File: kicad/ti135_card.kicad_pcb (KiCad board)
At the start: 8 copper layers, 76 x 65.1 mm, 395 parts, among them J1 JTAG 3.3V, J101 5V0 bench input, J2 UART 3.3V, J3 2x19 1.27mm socket (bottom), J5 LCD 1x14 2.54mm, J6 2x3 1.27mm (bottom), J9 HR911130A, U1001 THGAMVG7T13BAIL, U101 NCP163ASN330T1G, U1201 SN74AXC8T245PWR, U1202 SN74AXC8T245PWR, U1203 SN74AXC8T245PWR, U1204 SN74AXC8T245PWR, U1301 SN74LV4051APWR, U1302 OPA365AIDBVR, U1303 ADS7056IRUGR, U1304 OPA365AIDBVR, U1305 OPA365AIDBVR, U1306 OPA365AIDBVR, U201 TLV62585PDRLR, U301 TLV62585PDRLR, U311 TLV62585PDRLR, U331 TLV62585PDRLR, U341 TLV62585PDRLR, U401 TPS3808G01DBVR, U501 Ti135N484I3, U601 IS25WP128-RHLE, U801 H9HCNNN8KUMLHR-NME, U901 RTL8211FDI-CG, U902 74LVC1G07GW, Y701 OT322525MJBA4SL, Y901 25MHz

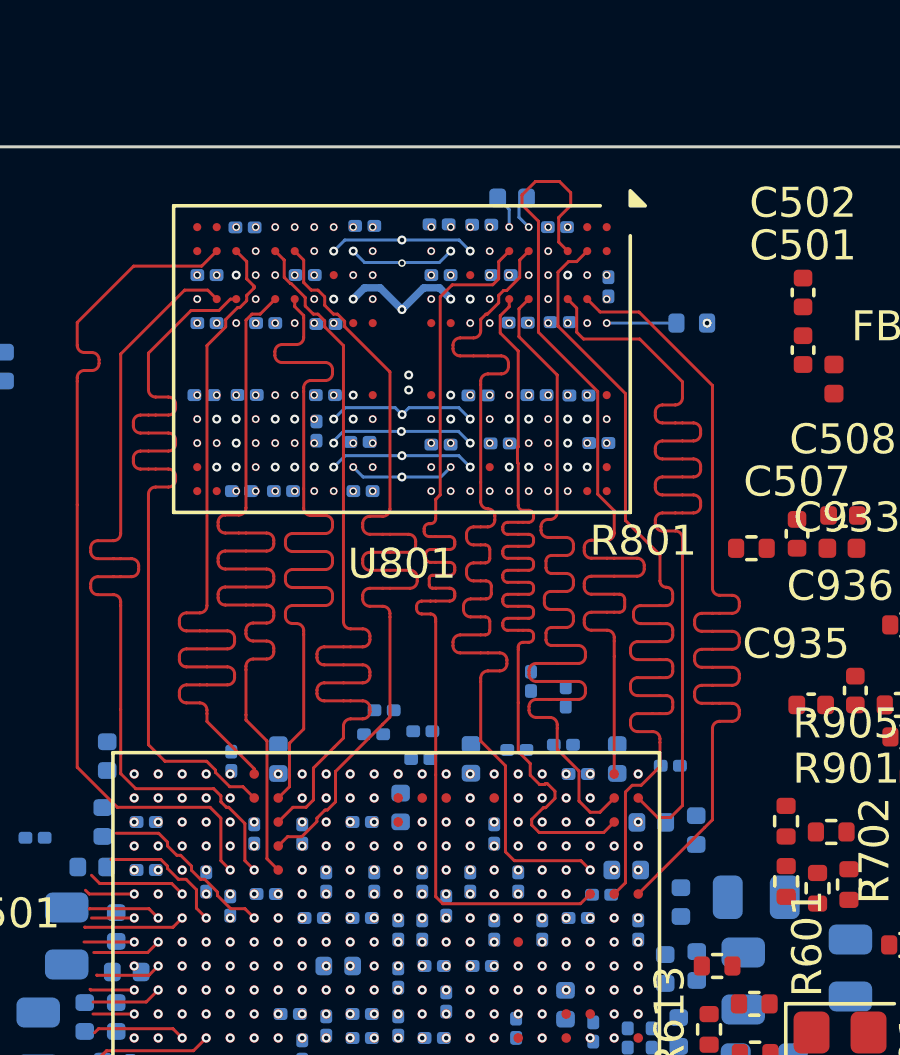
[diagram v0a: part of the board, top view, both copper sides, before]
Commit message: LPDDR4 tuned: all delay windows and crosstalk spacing pass DRC
Board (hand tuning with pcbnew tuning patterns, 52 patterns):
- CA/CKE/CS vs CK -1.8..+0.8 ps (rule +-5.3), CK P/N 0.24 ps.
- DQ - DQS: byte 0 +9.0..11.8, byte 1 +8.9..13.2, byte 2 +11.1..12.1, byte 3 +11.2..14.9 ps (window +5..+15).
  Byte 1's DQS raised to 211.8 ps (dq15 - 10) instead of shortening its long DQs.
- Removed three in-pad vias on dq2/dq16/dq23 (F.Cu-only nets: the barrel was a stub).
- DRC (zones refilled): no clearance, length or skew errors; all LPDDR4 nets connected.

Rules and tools:
- ddr_timing.py: per-net tuner offset on shared nets (tuner - path, read from each pattern's last_tuning_length:
  CA1 +11 ps, CK +2..3 ps), so "Update all tuning patterns" puts the real path on target; DQS_FLOOR for byte 1.
- lpddr_xtalk_spacing/group are errors, exempt P/N of one pair only (isCoupledDiffPair) and the BGAs only when both
  items touch the same courtyard: tested on A alone, a long segment starting under U801 gave every meander beside it
  0.1 mm along its whole length.
- LPDDR4 netclass clearance 0.2 mm (.kicad_pro) as a backstop, with DRC exceptions to 0.1 mm under the BGAs,
  within a pair and to non-LPDDR4 copper.
- kicad_ibis_simulation: DELAY_RULES.md tuner configuration and spacing notes.

Co-Authored-By: Claude Opus 5.5 <noreply@anthropic.com>
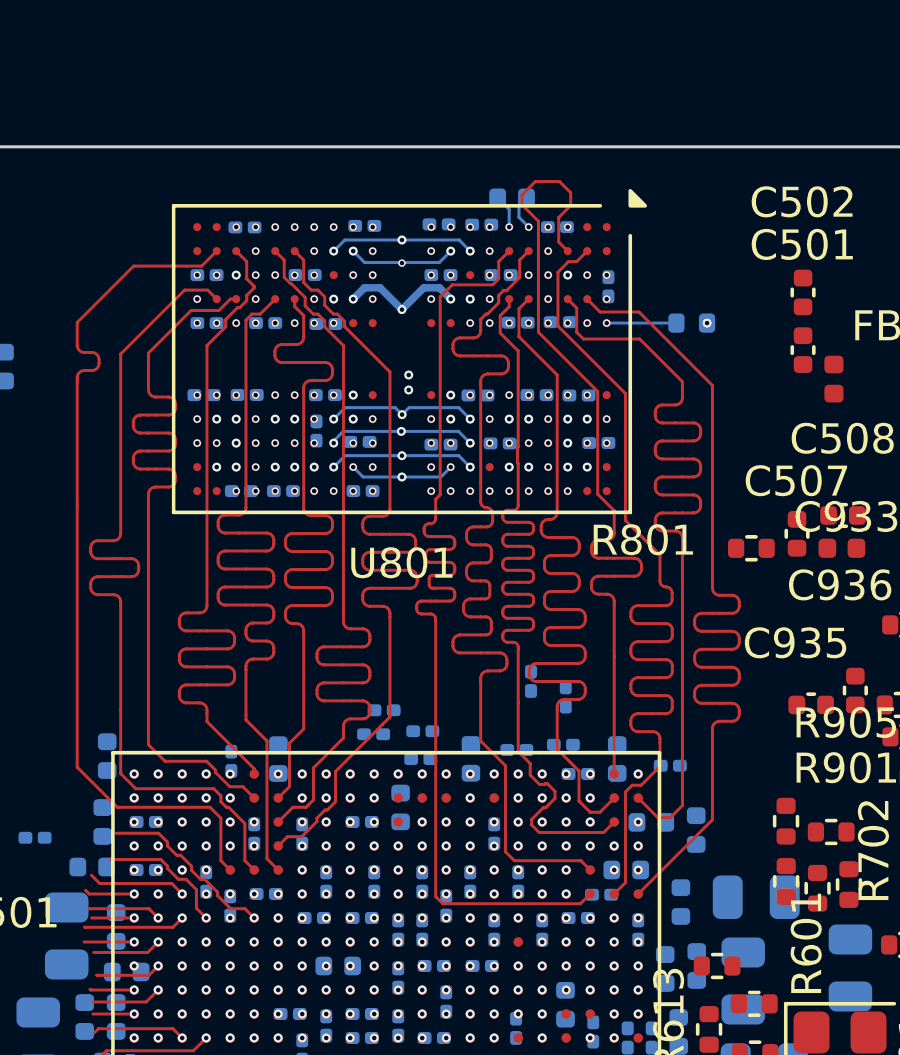
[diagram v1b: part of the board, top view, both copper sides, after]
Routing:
- net /08 lpddr4/ddr_dq10: track 13.3 -> 17.6 mm
- net /08 lpddr4/ddr_dq11: track 14.5 -> 18.8 mm
- net /08 lpddr4/ddr_dq12: track 14.1 -> 18.3 mm
- net /08 lpddr4/ddr_dqs1_N: track 14.3 -> 18.4 mm
- net /08 lpddr4/ddr_dqs1_P: track 14.3 -> 18.4 mm
- net /08 lpddr4/ddr_dq31: track 22.3 -> 18.7 mm
- net /08 lpddr4/ddr_dq1: track 32.2 -> 28.7 mm
- net /08 lpddr4/ddr_dq13: track 16.7 -> 19.8 mm
- net /08 lpddr4/ddr_dq30: track 20.9 -> 18.1 mm
- net /08 lpddr4/ddr_dm0: track 29.6 -> 27.3 mm
- net /08 lpddr4/ddr_dq14: track 16.1 -> 18.2 mm
- net /08 lpddr4/ddr_ca1: track 32.1 -> 34.1 mm
- net /08 lpddr4/ddr_dq8: track 17.3 -> 19.0 mm
- net /08 lpddr4/ddr_dq15: track 20.8 -> 19.8 mm
- net /08 lpddr4/ddr_dm1: track 19.7 -> 18.7 mm
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
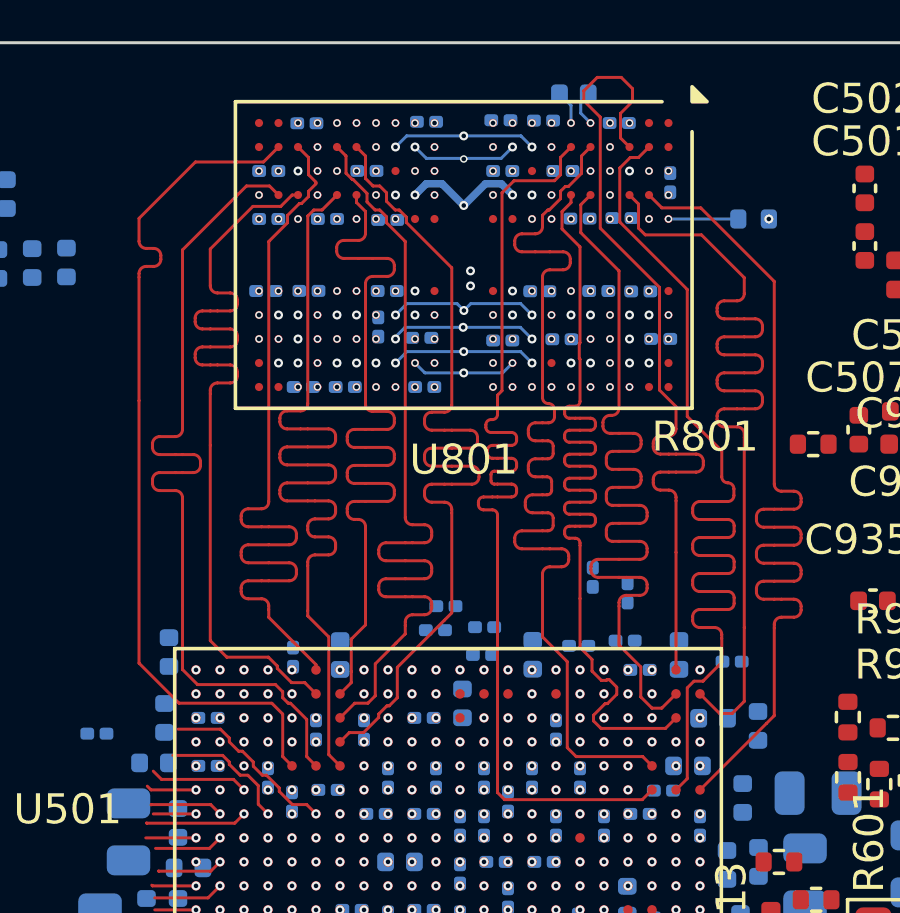
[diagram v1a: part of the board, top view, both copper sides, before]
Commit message: CKE: 10 ohm series resistor R803 on B.Cu at the U501 CKE via
Sheet 08: U501 AB11 -> ddr_cke0_fpga -> R803 (10R 0402, C25077) -> ddr_cke0 -> U801 J4/P4; lpddr_ca netclass
pattern includes cke0_fpga. CKE has no ODT; at max corner / 3200 Mbps it peaked 16 mV over the overshoot limit,
with the resistor 179 mV under it (sim/lpddr4_si/results/routed_corners.md). Board: R803 placed on B.Cu on the
CKE via (user), CKE rerouted to it.

Co-Authored-By: Claude Opus 5.5 <noreply@anthropic.com>
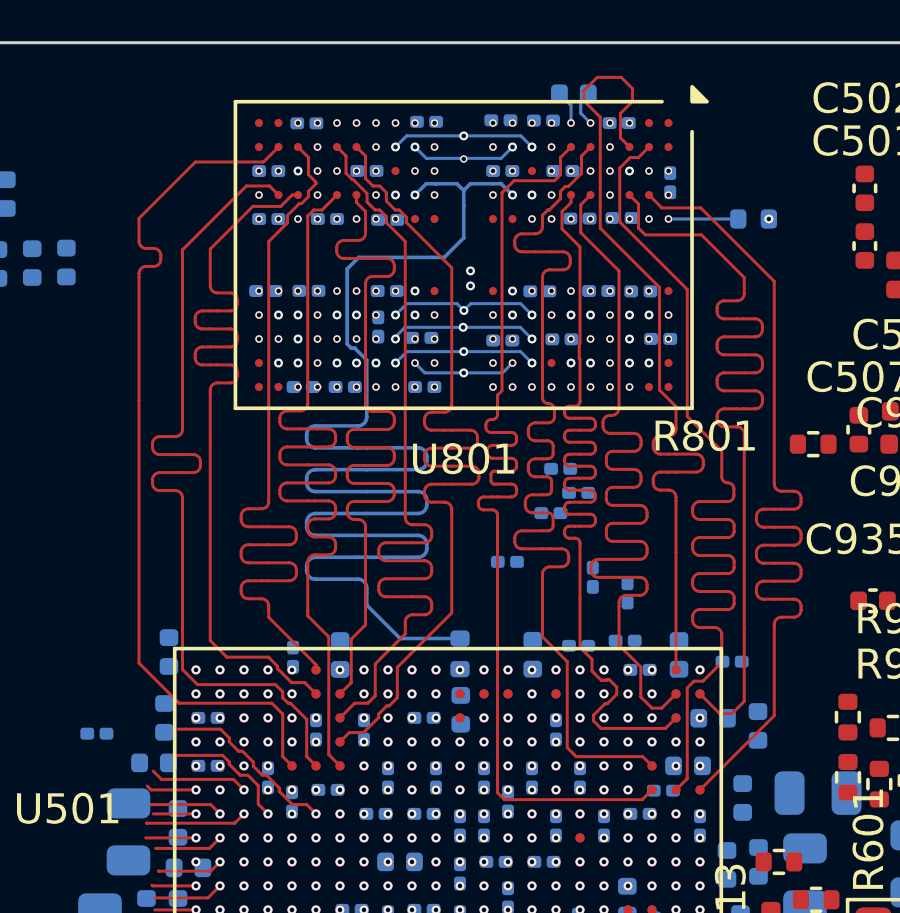
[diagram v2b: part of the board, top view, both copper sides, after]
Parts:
- added R803: 10R, Resistor_SMD:R_0402_1005Metric, B.Cu at (164.4, 72.1)
- moved C5060 6.73 mm to (167.8, 65.9)
- moved C5072 5.82 mm to (168.4, 66.7)
- moved C5073 5.48 mm to (167.4, 67.4)
- moved C5062 2.30 mm to (166.0, 69.0)
- moved C530 0.22 mm to (164.4, 73.9)
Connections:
- U501 pad AB11: /08 lpddr4/ddr_cke0 -> /08 lpddr4/ddr_cke0_fpga
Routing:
- net /08 lpddr4/ddr_cke0: track 35.2 -> 50.6 mm, vias 4 -> 2
- net /08 lpddr4/ddr_cke0_fpga: vias 0 -> 1
